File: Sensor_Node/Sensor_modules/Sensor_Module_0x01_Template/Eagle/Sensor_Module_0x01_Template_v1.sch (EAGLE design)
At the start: 14 parts, among them J1 M04_SMD_90, J4 ARDUINO_ISP, U2 ATMEGA328P_TQFP, Y1 8MHZ

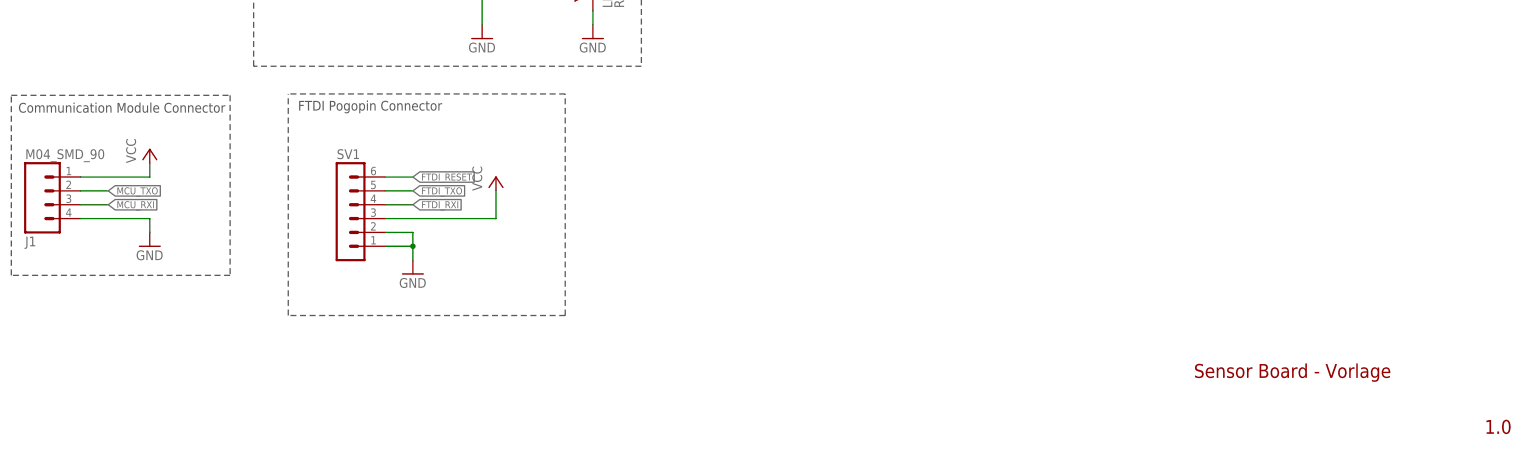
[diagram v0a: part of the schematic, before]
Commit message: Renaming boards to modules inside eagle files
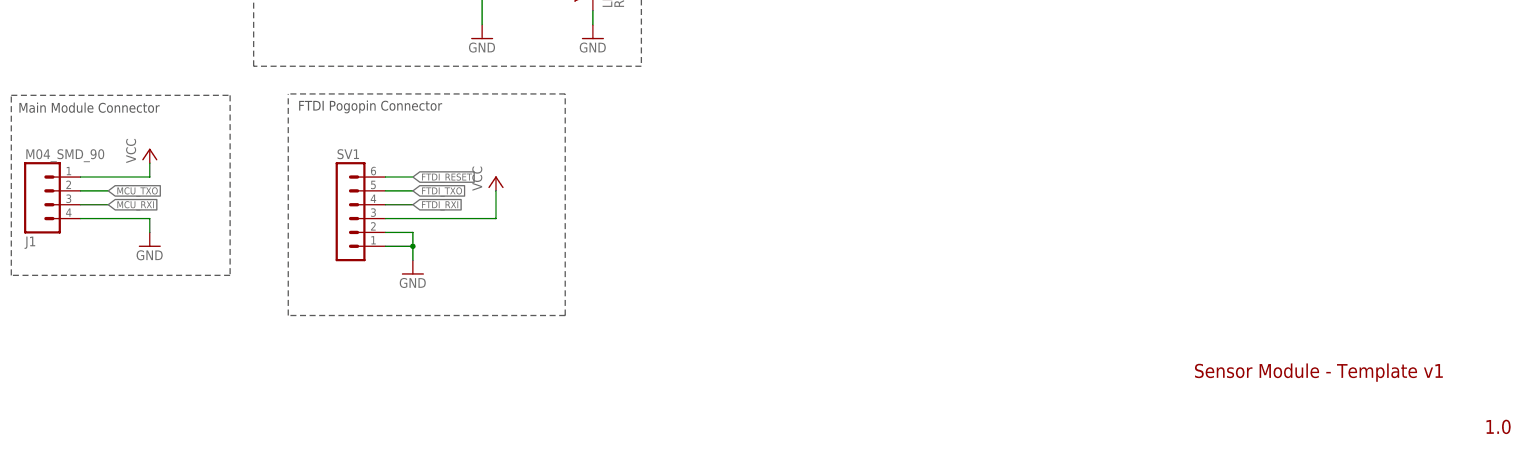
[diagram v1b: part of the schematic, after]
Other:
- note added: "Main Module Connector"
- note added: "Sensor Module - Template v1"
- note removed: "Communication Module Connector"
- note removed: "Sensor Board - Vorlage"
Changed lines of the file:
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@@
 <?xml version="1.0" encoding="utf-8"?>
 <!DOCTYPE eagle SYSTEM "eagle.dtd">
-<eagle version="8.4.3">
+<eagle version="9.1.1">
 <drawing>
 <settings>
@@
 <wire x1="47.752" y1="63.246" x2="47.752" y2="30.226" width="0.1524" layer="97" style="shortdash"/>
 <wire x1="47.752" y1="30.226" x2="7.62" y2="30.226" width="0.1524" layer="97" style="shortdash"/>
-<text x="8.89" y="60.071" size="1.778" layer="97">Communication Module Connector</text>
-<text x="224.527240625" y="11.421534375" size="2.54" layer="94" font="vector">Sensor Board - Vorlage</text>
+<text x="8.89" y="60.071" size="1.778" layer="97">Main Module Connector</text>
+<text x="224.527240625" y="11.421534375" size="2.54" layer="94" font="vector">Sensor Module - Template v1</text>
 <text x="277.8550125" y="1.158059375" size="2.54" layer="94" font="vector">1.0</text>
 <wire x1="109.22" y1="63.5" x2="58.42" y2="63.5" width="0.1524" layer="97" style="shortdash"/>
